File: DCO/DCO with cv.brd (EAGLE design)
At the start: 45.7 x 19 mm, 24 parts, among them IC1 PIC16F18325SL, IC2 MAX5216, IC3 TL082D, IC4 TL082D, Q1 MMBT3906

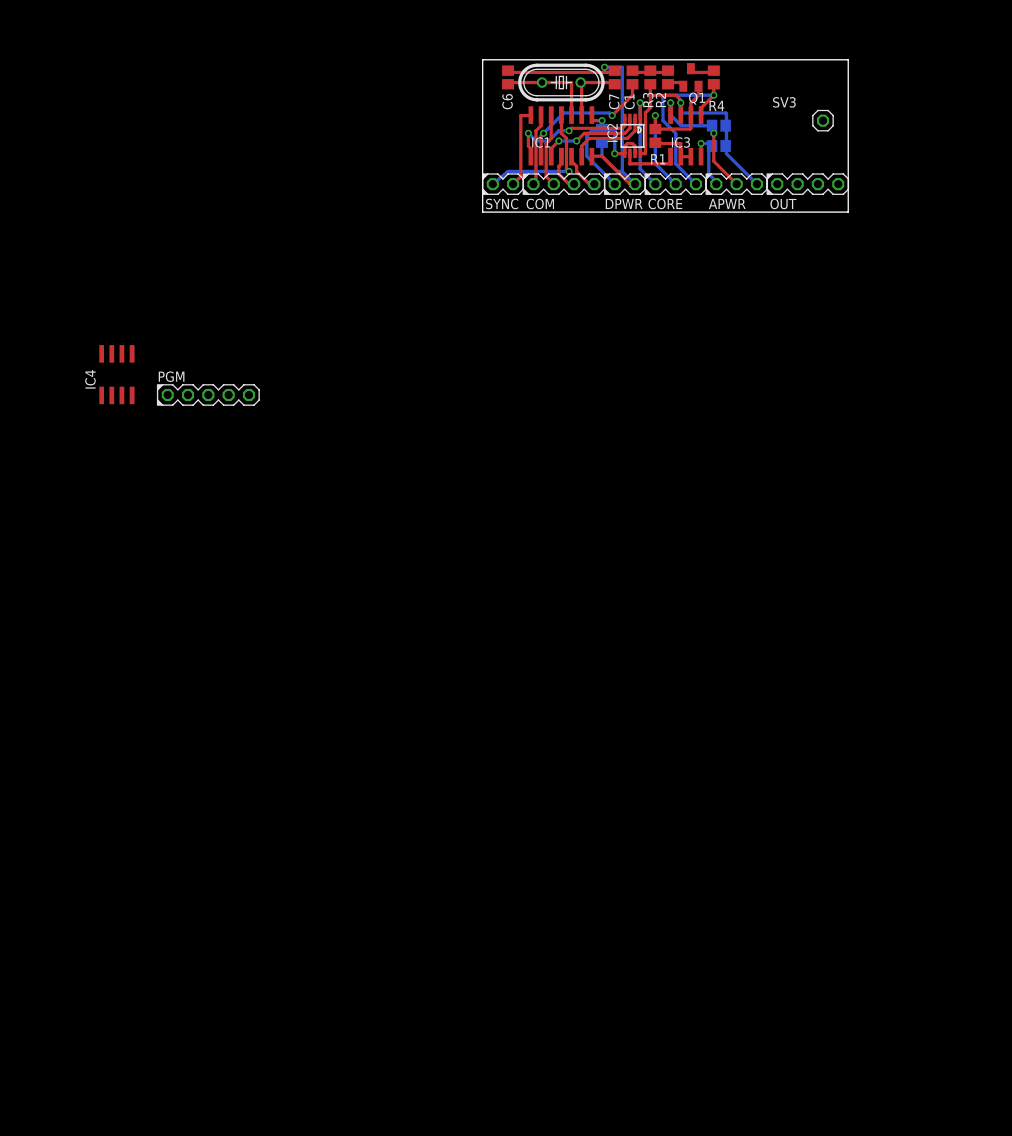
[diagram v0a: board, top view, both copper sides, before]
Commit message: Partially complete layout for DCO with CV control for pulse and sub osc, and separate triangle wave former
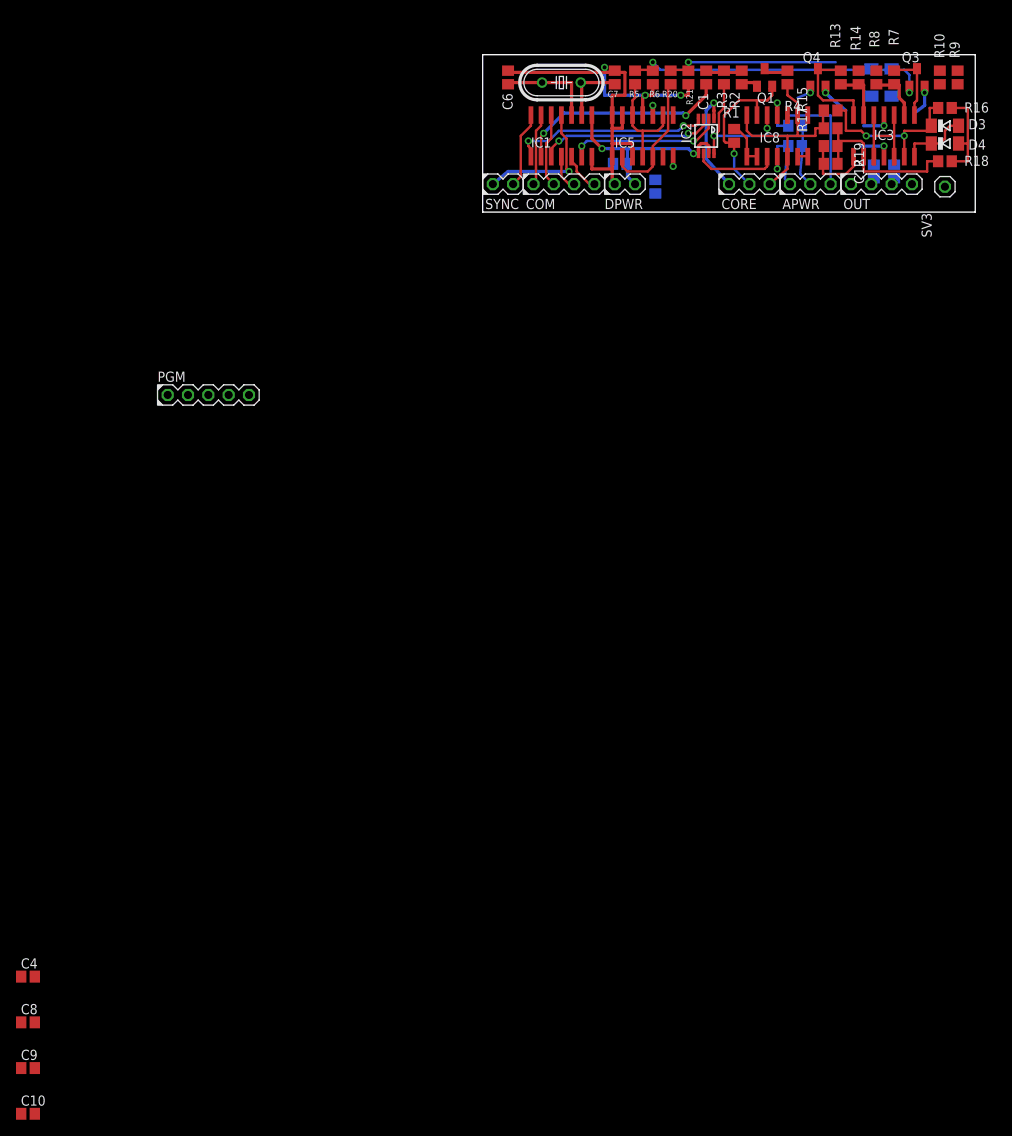
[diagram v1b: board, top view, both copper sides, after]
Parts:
- removed IC4: TL082D, linear:SO08
- added C10, C11, C12, C4, C8, C9: 100nF, resistor:C0805
- added D1, D2, D3, D4: (no value), diode:SOD80C
- added IC5: 4013D, joakim:SO14J
- added IC8: TL074D, linear:SO14
- added Q3, Q4: MMBT3906, transistor-pnp:SOT23-BEC
- added R10: 22k, resistor:R0805
- added R11, R20, R5: 68k, resistor:R0805
- added R12: 56k, resistor:R0805
- added R13, R14, R7, R8: (no value), resistor:R0805
- added R15, R16, R17, R18, R9: 100k, resistor:R0805
- added R19: 200k, resistor:R0805
- added R21, R6: 330k, resistor:R0805
- IC3: value TL082D -> TL074D; device linear:SO08 -> linear:SO14
- moved IC3 24.8 mm to (50.2, 9.53)
- moved SV3 17.3 mm to (57.8, 3.17), turned to 90 degrees
- moved C2 9.86 mm to (39.1, 10.8)
- moved C3 9.86 mm to (39.1, 8.26)
- moved R1 9.84 mm to (31.4, 9.53), turned to 270 degrees
- moved APWR 9.21 mm to (41.0, 3.49)
- moved R3 9.21 mm to (30.2, 16.8)
- moved R4 9.21 mm to (38.1, 16.8)
- moved C1 9.21 mm to (27.9, 16.8)
- moved CORE 9.21 mm to (33.3, 3.49)
- moved IC2 9.21 mm to (27.9, 9.53)
- moved Q1 9.21 mm to (35.2, 16.8)
- moved R2 9.21 mm to (32.4, 16.8)
- moved OUT 9.21 mm to (49.8, 3.49)
- moved C5 4.14 mm to (17.1, 6.03), turned to 0 degrees
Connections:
- removed net PWM: IC4.3, SV3.1
- removed net V+: IC4.8
- removed net V-: IC4.4
- new net +15V1: C4.1
- new net +15V2: C9.1
- new net -15V1: C8.2
- new net -15V2: C10.2
- new net N$1: R20.2, R21.2
- new net N$11: Q3.B, R5.2, R6.2
- new net N$12: D1.C, IC3.1, Q3.C, R7.2
- new net N$13: IC8.1, R9.1
- new net N$14: Q4.B, R10.2, R9.2
- new net N$15: IC3.2, R7.1, R8.2
- new net N$16: D2.C, IC3.7, Q4.C, R13.2
- new net N$17: D1.A, R11.1
- new net N$18: D2.A, R12.1
- new net N$19: D3.C, IC3.13, R15.2, R16.1
- new net N$20: IC3.6, R13.1, R14.2
- new net N$23: D3.A, D4.C, IC3.14
- new net N$24: D4.A, R16.2, R18.2
- new net PULSE_CV: R14.1
- new net PWM_CV: IC8.3, SV3.1
- new net SUB_1OCT: IC5.11, IC5.2, IC5.5, R5.1
- new net SUB_2OCT: IC5.12, IC5.9, R20.1
- new net SUB_OSC_CV: R8.1
- new net TRI_OUT: C12.2, IC3.8, R19.2
- new net TRI_SYM: C12.1, IC3.9, R17.2, R18.1, R19.1
- net +15V: now also APWR.3, IC3.4, IC8.4; no longer APWR.1, IC3.8
- net +5V: now also C11.1, DPWR.2, IC5.14; no longer DPWR.1
- net -15V: now also APWR.1, IC3.11, IC8.11; no longer APWR.2, IC3.4
- net AGND: now also APWR.2, C10.1, C4.2, C8.1, C9.2, IC3.10, IC3.12, IC3.5, IC8.5, Q3.E, Q4.E, R10.1; no longer APWR.3
- net CAP1: now also IC8.6; no longer IC3.2
- net CAP2: now also IC8.12, IC8.2, IC8.7, R15.1, R17.1; no longer IC3.1, IC4.2, IC4.5
- net CHARGE_VOLTAGE: now also IC8.10; no longer IC3.5
- net DGND: now also C11.2, DPWR.1, IC5.10, IC5.4, IC5.6, IC5.7, IC5.8, R21.1, R6.1; no longer DPWR.2
- net N$10: now also IC8.8, IC8.9; no longer IC3.6, IC3.7
- net PULSE_OUT: now also R12.2; no longer IC4.1
- net SAW_OUT: now also IC8.13, IC8.14; no longer IC4.6, IC4.7
- net SUB_OSC_OUT: now also R11.2
- net TIMER_OUT: now also IC5.3
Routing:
- net N$11: track 0.00 -> 39.2 mm, vias 0 -> 2
- net TRI_SYM: track 0.00 -> 22.1 mm
- net DGND: track 45.6 -> 67.5 mm, vias 1 -> 3
- net N$1: track 0.00 -> 21.8 mm, vias 0 -> 1
- net N$19: track 0.00 -> 21.7 mm, vias 0 -> 2
- net AGND: track 33.2 -> 52.0 mm, vias 1 -> 4
- net SUB_2OCT: track 0.00 -> 16.7 mm
- net +15V: track 9.27 -> 24.9 mm, vias 1 -> 2
- net SUB_1OCT: track 0.00 -> 14.2 mm
- net N$16: track 0.00 -> 12.8 mm
- net N$24: track 0.00 -> 11.8 mm
- net TIMER_OUT: track 17.8 -> 29.1 mm, vias 2 -> 3
- net TRI_OUT: track 0.00 -> 9.15 mm
- net DAC_SPI_CLOCK: track 13.1 -> 22.2 mm
- net DAC_CS: track 10.3 -> 19.4 mm, vias 0 -> 2
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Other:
- board size 45.7 x 19 mm -> 61.6 x 19.7 mm

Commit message: Finished layout of DCO core v1.0
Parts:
- R18: value 100k -> 50k
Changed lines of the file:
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@@
 <attribute name="VALUE" x="42.7355" y="8.1915" size="1.27" layer="27"/>
 </element>
-<element name="R18" library="resistor" package="R0805" value="100k" x="57.785" y="6.35" smashed="yes">
+<element name="R18" library="resistor" package="R0805" value="50k" x="57.785" y="6.35" smashed="yes">
 <attribute name="NAME" x="60.198" y="5.7785" size="1.27" layer="25"/>
 <attribute name="VALUE" x="57.023" y="4.064" size="1.27" layer="27"/>
